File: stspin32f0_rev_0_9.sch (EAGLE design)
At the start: 83 parts, among them IC1 STSPIN32F0, J1 2X6 FEMALE, Q1 IPD088N06N3_G, Q2 IPD088N06N3_G, Q3 IPD088N06N3_G, Q4 IPD088N06N3_G, Q5 IPD088N06N3_G, Q6 IPD088N06N3_G

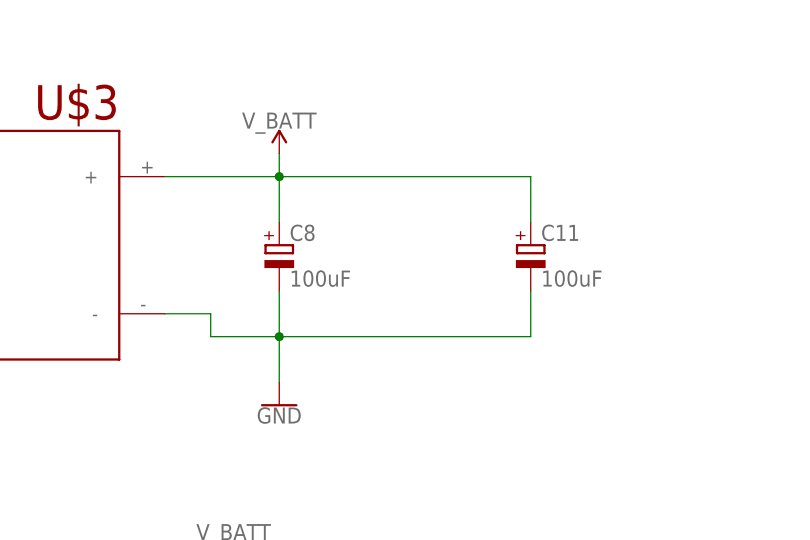
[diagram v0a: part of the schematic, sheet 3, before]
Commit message: routing done and drc cleared
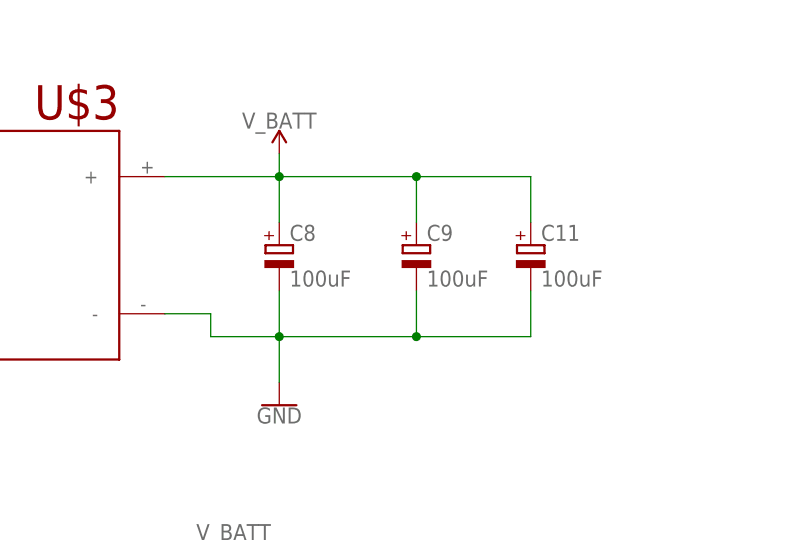
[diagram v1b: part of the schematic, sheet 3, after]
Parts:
- added C9: 100uF, rcl:CPOL-EUUD-6,3X7,7
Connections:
- net GND: now also C9.-
- net V_BATT: now also C9.+
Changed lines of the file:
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@@
 <part name="GND23" library="SparkFun-PowerSymbols" deviceset="GND" device=""/>
 <part name="GND24" library="SparkFun-PowerSymbols" deviceset="GND" device=""/>
+<part name="C9" library="rcl" library_urn="urn:adsk.eagle:library:334" deviceset="CPOL-EU" device="UD-6,3X7,7" value="100uF"/>
 </parts>
 <sheets>
@@
 <instance part="R37" gate="G$1" x="220.98" y="68.58"/>
 <instance part="R38" gate="G$1" x="215.9" y="160.02"/>
+<instance part="C9" gate="G$1" x="58.42" y="152.4"/>
 </instances>
 <busses>
@@
 <wire x1="43.18" y1="160.02" x2="43.18" y2="154.94" width="0.1524" layer="91"/>
 <wire x1="71.12" y1="154.94" x2="71.12" y2="160.02" width="0.1524" layer="91"/>
-<wire x1="71.12" y1="160.02" x2="43.18" y2="160.02" width="0.1524" layer="91"/>
+<wire x1="71.12" y1="160.02" x2="58.42" y2="160.02" width="0.1524" layer="91"/>
 <junction x="43.18" y="160.02"/>
 <pinref part="U$3" gate="G$1" pin="+"/>
+<wire x1="58.42" y1="160.02" x2="43.18" y2="160.02" width="0.1524" layer="91"/>
 <wire x1="30.48" y1="160.02" x2="43.18" y2="160.02" width="0.1524" layer="91"/>
+<pinref part="C9" gate="G$1" pin="+"/>
+<wire x1="58.42" y1="154.94" x2="58.42" y2="160.02" width="0.1524" layer="91"/>
+<junction x="58.42" y="160.02"/>
 </segment>
 </net>
@@
 <pinref part="C11" gate="G$1" pin="-"/>
 <wire x1="43.18" y1="142.24" x2="43.18" y2="137.16" width="0.1524" layer="91"/>
-<wire x1="43.18" y1="142.24" x2="71.12" y2="142.24" width="0.1524" layer="91"/>
+<wire x1="43.18" y1="142.24" x2="58.42" y2="142.24" width="0.1524" layer="91"/>
+<wire x1="58.42" y1="142.24" x2="71.12" y2="142.24" width="0.1524" layer="91"/>
 <wire x1="71.12" y1="142.24" x2="71.12" y2="147.32" width="0.1524" layer="91"/>
 <junction x="43.18" y="142.24"/>
@@
 <pinref part="U$3" gate="G$1" pin="-"/>
 <wire x1="30.48" y1="144.78" x2="35.56" y2="144.78" width="0.1524" layer="91"/>
-</segment>
-<segment>
+<pinref part="C9" gate="G$1" pin="-"/>
+<wire x1="58.42" y1="147.32" x2="58.42" y2="142.24" width="0.1524" layer="91"/>
+<junction x="58.42" y="142.24"/>
+</segment>
+<segment>

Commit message: fixed names
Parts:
- renumbered J1 to IO, U$1 to PROG
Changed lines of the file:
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@@
 <part name="C14" library="wiral" deviceset="CAP-25V-20%" device="-0603" value="100pF"/>
 <part name="R15" library="wiral" deviceset="RES-1/10W-5%-" device="0603" value="560R"/>
-<part name="U$1" library="wiral" deviceset="SWD_PROG_POGO" device=""/>
+<part name="PROG" library="wiral" deviceset="SWD_PROG_POGO" device=""/>
 <part name="SUPPLY9" library="SparkFun-PowerSymbols" deviceset="3.3V" device=""/>
 <part name="GND13" library="SparkFun-PowerSymbols" deviceset="GND" device=""/>
@@
 <part name="Q5" library="inventas" deviceset="IPD088N06N3_G" device=""/>
 <part name="Q6" library="inventas" deviceset="IPD088N06N3_G" device=""/>
-<part name="J1" library="SparkFun-Connectors" deviceset="CONN_06X2" device="PTH_FEMALE" value="2X6 FEMALE"/>
+<part name="IO" library="SparkFun-Connectors" deviceset="CONN_06X2" device="PTH_FEMALE" value="2X6 FEMALE"/>
 <part name="SUPPLY18" library="SparkFun-PowerSymbols" deviceset="3.3V" device=""/>
 <part name="GND23" library="SparkFun-PowerSymbols" deviceset="GND" device=""/>
@@
 <instance part="SUPPLY8" gate="G$1" x="25.4" y="48.26"/>
 <instance part="GND12" gate="1" x="25.4" y="15.24"/>
-<instance part="U$1" gate="G$1" x="208.28" y="149.86"/>
+<instance part="PROG" gate="G$1" x="208.28" y="149.86"/>
 <instance part="SUPPLY9" gate="G$1" x="193.04" y="157.48"/>
 <instance part="GND13" gate="1" x="193.04" y="139.7"/>
@@
 <instance part="C16" gate="G$1" x="10.16" y="116.84"/>
 <instance part="C22" gate="G$1" x="154.94" y="96.52" rot="R90"/>
-<instance part="J1" gate="G$1" x="218.44" y="88.9"/>
+<instance part="IO" gate="G$1" x="218.44" y="88.9"/>
 <instance part="SUPPLY18" gate="G$1" x="231.14" y="104.14"/>
 <instance part="GND23" gate="1" x="210.82" y="106.68" rot="R180"/>
@@
 </segment>
 <segment>
-<pinref part="U$1" gate="G$1" pin="VDD"/>
+<pinref part="PROG" gate="G$1" pin="VDD"/>
 <pinref part="SUPPLY9" gate="G$1" pin="3.3V"/>
 <wire x1="195.58" y1="154.94" x2="193.04" y2="154.94" width="0.1524" layer="91"/>
@@
 </segment>
 <segment>
-<pinref part="J1" gate="G$1" pin="2"/>
+<pinref part="IO" gate="G$1" pin="2"/>
 <pinref part="SUPPLY18" gate="G$1" pin="3.3V"/>
 <wire x1="228.6" y1="101.6" x2="231.14" y2="101.6" width="0.1524" layer="91"/>
@@
 </segment>
 <segment>
-<pinref part="U$1" gate="G$1" pin="GND"/>
+<pinref part="PROG" gate="G$1" pin="GND"/>
 <pinref part="GND13" gate="1" pin="GND"/>
 <wire x1="195.58" y1="144.78" x2="193.04" y2="144.78" width="0.1524" layer="91"/>
@@
 </segment>
 <segment>
-<pinref part="J1" gate="G$1" pin="1"/>
+<pinref part="IO" gate="G$1" pin="1"/>
 <wire x1="213.36" y1="101.6" x2="210.82" y2="101.6" width="0.1524" layer="91"/>
 <wire x1="210.82" y1="101.6" x2="210.82" y2="104.14" width="0.1524" layer="91"/>
@@
 </segment>
 <segment>
-<pinref part="J1" gate="G$1" pin="11"/>
+<pinref part="IO" gate="G$1" pin="11"/>
 <pinref part="GND24" gate="1" pin="GND"/>
 <wire x1="213.36" y1="88.9" x2="208.28" y2="88.9" width="0.1524" layer="91"/>
@@
 </segment>
 <segment>
-<pinref part="U$1" gate="G$1" pin="RST"/>
+<pinref part="PROG" gate="G$1" pin="RST"/>
 <wire x1="195.58" y1="149.86" x2="190.5" y2="149.86" width="0.1524" layer="91"/>
 <label x="190.5" y="149.86" size="1.778" layer="95" rot="R180" xref="yes"/>
@@
 </segment>
 <segment>
-<pinref part="J1" gate="G$1" pin="7"/>
+<pinref part="IO" gate="G$1" pin="7"/>
 <wire x1="213.36" y1="93.98" x2="210.82" y2="93.98" width="0.1524" layer="91"/>
 <label x="210.82" y="93.98" size="1.27" layer="95" rot="R180" xref="yes"/>
@@
 </segment>
 <segment>
-<pinref part="J1" gate="G$1" pin="8"/>
+<pinref part="IO" gate="G$1" pin="8"/>
 <wire x1="228.6" y1="93.98" x2="231.14" y2="93.98" width="0.1524" layer="91"/>
 <label x="231.14" y="93.98" size="1.27" layer="95" xref="yes"/>
@@
 </segment>
 <segment>
-<pinref part="U$1" gate="G$1" pin="SWCLK"/>
+<pinref part="PROG" gate="G$1" pin="SWCLK"/>
 <wire x1="223.52" y1="149.86" x2="228.6" y2="149.86" width="0.1524" layer="91"/>
 <label x="228.6" y="149.86" size="1.778" layer="95" xref="yes"/>
@@
 </segment>
 <segment>
-<pinref part="U$1" gate="G$1" pin="SWDIO"/>
+<pinref part="PROG" gate="G$1" pin="SWDIO"/>
 <wire x1="223.52" y1="154.94" x2="228.6" y2="154.94" width="0.1524" layer="91"/>
 <label x="228.6" y="154.94" size="1.778" layer="95" xref="yes"/>
@@
 </segment>
 <segment>
-<pinref part="J1" gate="G$1" pin="5"/>
+<pinref part="IO" gate="G$1" pin="5"/>
 <wire x1="213.36" y1="96.52" x2="210.82" y2="96.52" width="0.1524" layer="91"/>
 <label x="210.82" y="96.52" size="1.27" layer="95" rot="R180" xref="yes"/>
@@
 </segment>
 <segment>
-<pinref part="J1" gate="G$1" pin="6"/>
+<pinref part="IO" gate="G$1" pin="6"/>
 <wire x1="228.6" y1="96.52" x2="231.14" y2="96.52" width="0.1524" layer="91"/>
 <label x="231.14" y="96.52" size="1.27" layer="95" xref="yes"/>
@@
 </segment>
 <segment>
-<pinref part="J1" gate="G$1" pin="3"/>
+<pinref part="IO" gate="G$1" pin="3"/>
 <wire x1="213.36" y1="99.06" x2="210.82" y2="99.06" width="0.1524" layer="91"/>
 <label x="210.82" y="99.06" size="1.27" layer="95" rot="R180" xref="yes"/>
@@
 </segment>
 <segment>
-<pinref part="J1" gate="G$1" pin="4"/>
+<pinref part="IO" gate="G$1" pin="4"/>
 <wire x1="228.6" y1="99.06" x2="231.14" y2="99.06" width="0.1524" layer="91"/>
 <label x="231.14" y="99.06" size="1.27" layer="95" xref="yes"/>
@@
 </segment>
 <segment>
-<pinref part="J1" gate="G$1" pin="10"/>
+<pinref part="IO" gate="G$1" pin="10"/>
 <wire x1="228.6" y1="91.44" x2="231.14" y2="91.44" width="0.1524" layer="91"/>
 <label x="231.14" y="91.44" size="1.27" layer="95" xref="yes"/>
@@
 </segment>
 <segment>
-<pinref part="J1" gate="G$1" pin="9"/>
+<pinref part="IO" gate="G$1" pin="9"/>
 <wire x1="213.36" y1="91.44" x2="210.82" y2="91.44" width="0.1524" layer="91"/>
 <label x="210.82" y="91.44" size="1.27" layer="95" rot="R180" xref="yes"/>
@@
 </segment>
 <segment>
-<pinref part="J1" gate="G$1" pin="12"/>
+<pinref part="IO" gate="G$1" pin="12"/>
 <wire x1="228.6" y1="88.9" x2="231.14" y2="88.9" width="0.1524" layer="91"/>
 <label x="231.14" y="88.9" size="1.27" layer="95" xref="yes"/>

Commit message: More vias and wider tracks for more current
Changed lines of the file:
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@@
 <part name="GND21" library="SparkFun-PowerSymbols" deviceset="GND" device=""/>
 <part name="U$3" library="wiral" deviceset="XT30" device=""/>
-<part name="FRAME4" library="SparkFun-Aesthetics" deviceset="FRAME-A4L" device=""/>
 <part name="ENC/HALL" library="SamacSys_Parts" deviceset="S5B-PH-SM4-TB(LF)(SN)" device=""/>
 <part name="SUPPLY17" library="SparkFun-PowerSymbols" deviceset="3.3V" device=""/>
@@
 <instance part="GND23" gate="1" x="210.82" y="106.68" rot="R180"/>
 <instance part="GND24" gate="1" x="208.28" y="83.82"/>
+<instance part="ENC/HALL" gate="G$1" x="205.74" y="43.18"/>
+<instance part="SUPPLY17" gate="G$1" x="200.66" y="53.34"/>
+<instance part="SUPPLY19" gate="G$1" x="185.42" y="53.34"/>
+<instance part="GND22" gate="1" x="198.12" y="30.48"/>
+<instance part="HALL/ENC_POWER" gate="G$1" x="193.04" y="50.8" rot="R90"/>
 </instances>
 <busses>
@@
 <wire x1="231.14" y1="101.6" x2="231.14" y2="104.14" width="0.1524" layer="91"/>
 </segment>
+<segment>
+<pinref part="HALL/ENC_POWER" gate="G$1" pin="3"/>
+<pinref part="SUPPLY17" gate="G$1" pin="3.3V"/>
+<wire x1="198.12" y1="50.8" x2="200.66" y2="50.8" width="0.1524" layer="91"/>
+<wire x1="200.66" y1="50.8" x2="200.66" y2="53.34" width="0.1524" layer="91"/>
+</segment>
 </net>
 <net name="GND" class="0">
@@
 <wire x1="213.36" y1="88.9" x2="208.28" y2="88.9" width="0.1524" layer="91"/>
 <wire x1="208.28" y1="88.9" x2="208.28" y2="86.36" width="0.1524" layer="91"/>
+</segment>
+<segment>
+<pinref part="ENC/HALL" gate="G$1" pin="5"/>
+<wire x1="205.74" y1="38.1" x2="198.12" y2="38.1" width="0.1524" layer="91"/>
+<pinref part="GND22" gate="1" pin="GND"/>
+<wire x1="198.12" y1="38.1" x2="198.12" y2="33.02" width="0.1524" layer="91"/>
 </segment>
 </net>
@@
 <wire x1="63.5" y1="142.24" x2="63.5" y2="139.7" width="0.1524" layer="91"/>
 </segment>
+<segment>
+<pinref part="HALL/ENC_POWER" gate="G$1" pin="1"/>
+<pinref part="SUPPLY19" gate="G$1" pin="12V"/>
+<wire x1="187.96" y1="50.8" x2="185.42" y2="50.8" width="0.1524" layer="91"/>
+<wire x1="185.42" y1="50.8" x2="185.42" y2="53.34" width="0.1524" layer="91"/>
+</segment>
 </net>
 <net name="NRST" class="0">
@@
 <label x="210.82" y="93.98" size="1.27" layer="95" rot="R180" xref="yes"/>
 </segment>
+<segment>
+<pinref part="ENC/HALL" gate="G$1" pin="3"/>
+<wire x1="205.74" y1="40.64" x2="200.66" y2="40.64" width="0.1524" layer="91"/>
+<label x="200.66" y="40.64" size="1.27" layer="95" rot="R180" xref="yes"/>
+</segment>
 </net>
 <net name="BATT_MEASURE" class="0">
@@
 <wire x1="228.6" y1="93.98" x2="231.14" y2="93.98" width="0.1524" layer="91"/>
 <label x="231.14" y="93.98" size="1.27" layer="95" xref="yes"/>
+</segment>
+<segment>
+<pinref part="ENC/HALL" gate="G$1" pin="2"/>
+<wire x1="226.06" y1="43.18" x2="231.14" y2="43.18" width="0.1524" layer="91"/>
+<label x="231.14" y="43.18" size="1.27" layer="95" xref="yes"/>
 </segment>
 </net>
@@
 <label x="231.14" y="91.44" size="1.27" layer="95" xref="yes"/>
 </segment>
+<segment>
+<pinref part="ENC/HALL" gate="G$1" pin="4"/>
+<wire x1="226.06" y1="40.64" x2="231.14" y2="40.64" width="0.1524" layer="91"/>
+<label x="231.14" y="40.64" size="1.27" layer="95" xref="yes"/>
+</segment>
 </net>
 <net name="PA3" class="0">
@@
 <wire x1="228.6" y1="88.9" x2="231.14" y2="88.9" width="0.1524" layer="91"/>
 <label x="231.14" y="88.9" size="1.27" layer="95" xref="yes"/>
+</segment>
+</net>
+<net name="N$22" class="0">
+<segment>
+<pinref part="ENC/HALL" gate="G$1" pin="1"/>
+<wire x1="205.74" y1="43.18" x2="193.04" y2="43.18" width="0.1524" layer="91"/>
+<wire x1="193.04" y1="43.18" x2="193.04" y2="45.72" width="0.1524" layer="91"/>
+<pinref part="HALL/ENC_POWER" gate="G$1" pin="2"/>
 </segment>
 </net>
@@
 </segment>
 </net>
-</nets>
-</sheet>
-<sheet>
-<plain>
-</plain>
-<instances>
-<instance part="FRAME4" gate="G$1" x="0" y="0"/>
-<instance part="ENC/HALL" gate="G$1" x="40.64" y="129.54"/>
-<instance part="SUPPLY17" gate="G$1" x="35.56" y="139.7"/>
-<instance part="SUPPLY19" gate="G$1" x="20.32" y="139.7"/>
-<instance part="GND22" gate="1" x="33.02" y="116.84"/>
-<instance part="HALL/ENC_POWER" gate="G$1" x="27.94" y="137.16" rot="R90"/>
-</instances>
-<busses>
-</busses>
-<nets>
-<net name="ENC_A/HALL1" class="0">
-<segment>
-<pinref part="ENC/HALL" gate="G$1" pin="2"/>
-<wire x1="60.96" y1="129.54" x2="66.04" y2="129.54" width="0.1524" layer="91"/>
-<label x="66.04" y="129.54" size="1.27" layer="95" xref="yes"/>
-</segment>
-</net>
-<net name="ENC_B/HALL2" class="0">
-<segment>
-<pinref part="ENC/HALL" gate="G$1" pin="3"/>
-<wire x1="40.64" y1="127" x2="35.56" y2="127" width="0.1524" layer="91"/>
-<label x="35.56" y="127" size="1.27" layer="95" rot="R180" xref="yes"/>
-</segment>
-</net>
-<net name="ENC_Z/HALL3" class="0">
-<segment>
-<pinref part="ENC/HALL" gate="G$1" pin="4"/>
-<wire x1="60.96" y1="127" x2="66.04" y2="127" width="0.1524" layer="91"/>
-<label x="66.04" y="127" size="1.27" layer="95" xref="yes"/>
-</segment>
-</net>
-<net name="GND" class="0">
-<segment>
-<pinref part="ENC/HALL" gate="G$1" pin="5"/>
-<wire x1="40.64" y1="124.46" x2="33.02" y2="124.46" width="0.1524" layer="91"/>
-<pinref part="GND22" gate="1" pin="GND"/>
-<wire x1="33.02" y1="124.46" x2="33.02" y2="119.38" width="0.1524" layer="91"/>
-</segment>
-</net>
-<net name="N$22" class="0">
-<segment>
-<pinref part="ENC/HALL" gate="G$1" pin="1"/>
-<wire x1="40.64" y1="129.54" x2="27.94" y2="129.54" width="0.1524" layer="91"/>
-<wire x1="27.94" y1="129.54" x2="27.94" y2="132.08" width="0.1524" layer="91"/>
-<pinref part="HALL/ENC_POWER" gate="G$1" pin="2"/>
-</segment>
-</net>
-<net name="12V" class="0">
-<segment>
-<pinref part="HALL/ENC_POWER" gate="G$1" pin="1"/>
-<pinref part="SUPPLY19" gate="G$1" pin="12V"/>
-<wire x1="22.86" y1="137.16" x2="20.32" y2="137.16" width="0.1524" layer="91"/>
-<wire x1="20.32" y1="137.16" x2="20.32" y2="139.7" width="0.1524" layer="91"/>
-</segment>
-</net>
-<net name="3.3V" class="0">
-<segment>
-<pinref part="HALL/ENC_POWER" gate="G$1" pin="3"/>
-<pinref part="SUPPLY17" gate="G$1" pin="3.3V"/>
-<wire x1="33.02" y1="137.16" x2="35.56" y2="137.16" width="0.1524" layer="91"/>
-<wire x1="35.56" y1="137.16" x2="35.56" y2="139.7" width="0.1524" layer="91"/>
-</segment>
-</net>
